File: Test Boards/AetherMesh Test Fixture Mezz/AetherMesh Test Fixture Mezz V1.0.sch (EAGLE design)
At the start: 7 parts, among them J1 POWER_JACKEJ508A, M1 AETHERMESH_MODULEMEZZ-HOLES

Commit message: Re-organized test fixture boards and corrected part number attributes
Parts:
- S1, S2: MFG# 4882 -> 9774040243R
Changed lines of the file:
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@@
 <?xml version="1.0" encoding="utf-8"?>
 <!DOCTYPE eagle SYSTEM "eagle.dtd">
-<eagle version="8.3.1">
+<eagle version="8.3.2">
 <drawing>
 <settings>
@@
 <part name="M1" library="AetherConnectivity" deviceset="AETHERMESH_MODULE" device="MEZZ-HOLES"/>
 <part name="S1" library="AetherConnectivity" deviceset="STANDOFF" device="WURTH">
-<attribute name="MFG#" value="4882"/>
+<attribute name="MFG#" value="9774040243R"/>
 </part>
 <part name="S2" library="AetherConnectivity" deviceset="STANDOFF" device="WURTH">
-<attribute name="MFG#" value="4882"/>
+<attribute name="MFG#" value="9774040243R"/>
 </part>
 <part name="GND2" library="3. growflux" library_urn="urn:adsk.eagle:library:207379" deviceset="GND" device=""/>

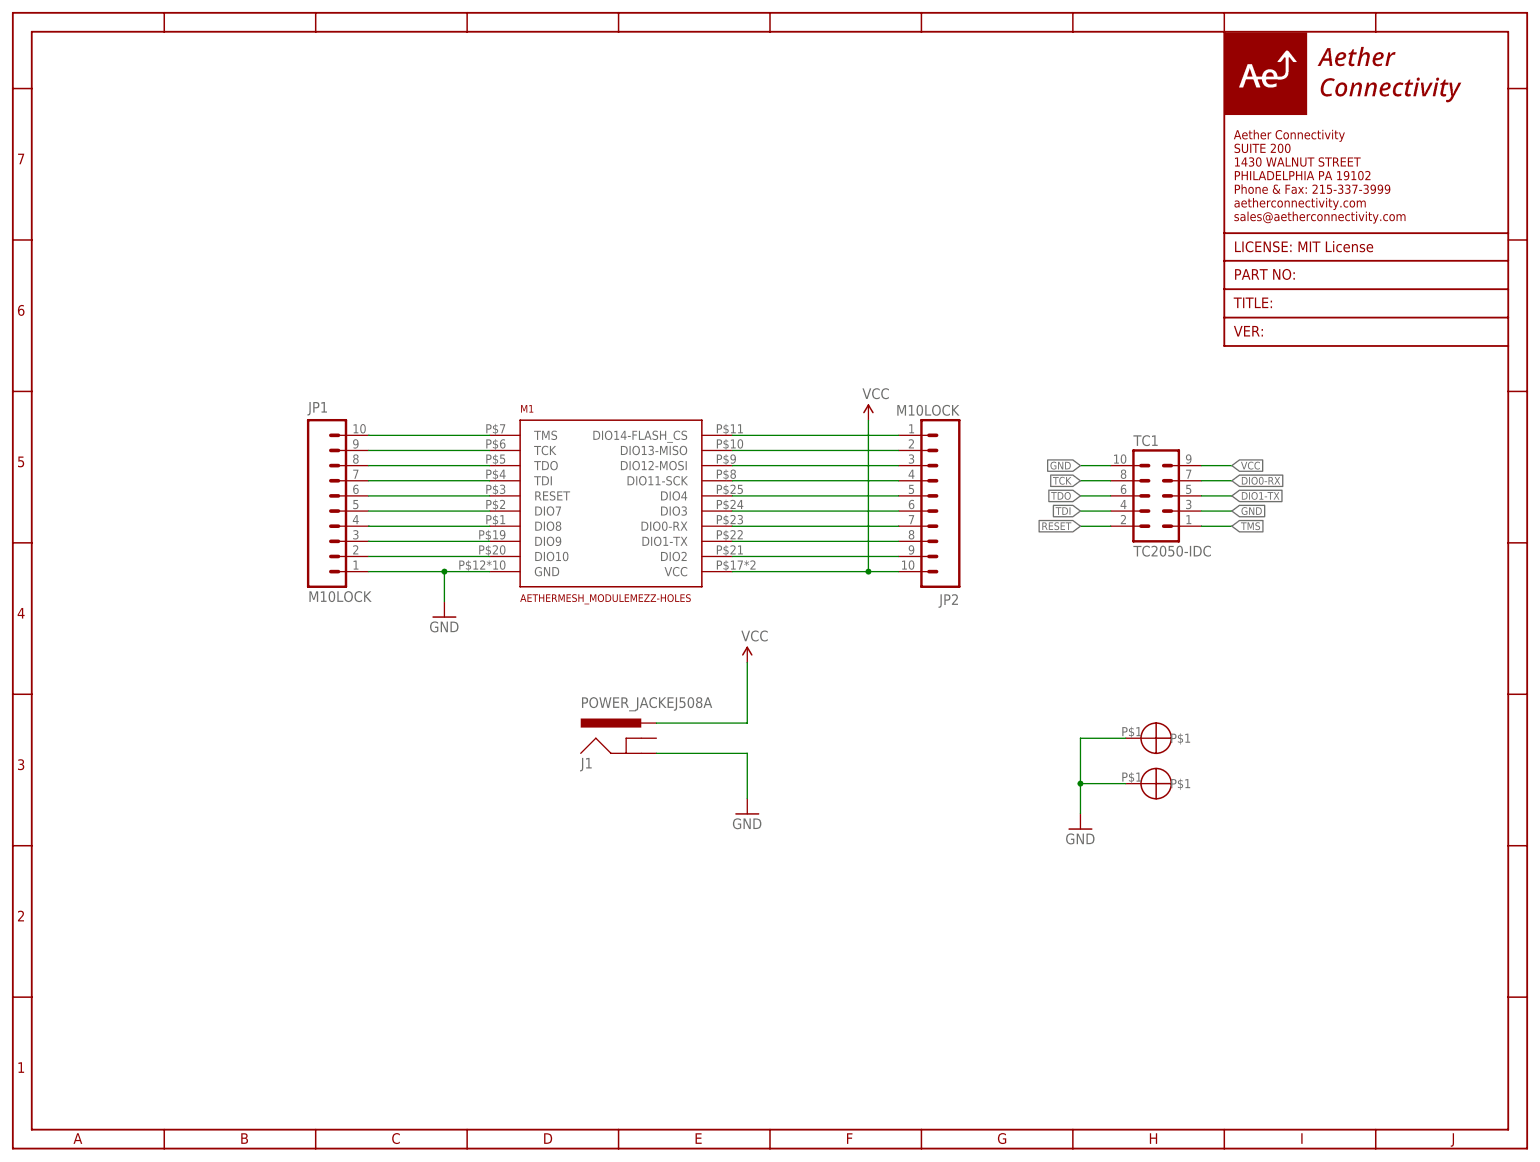
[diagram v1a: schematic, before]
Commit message: Updated test boards with silkscreen pin names and current measurment jumper
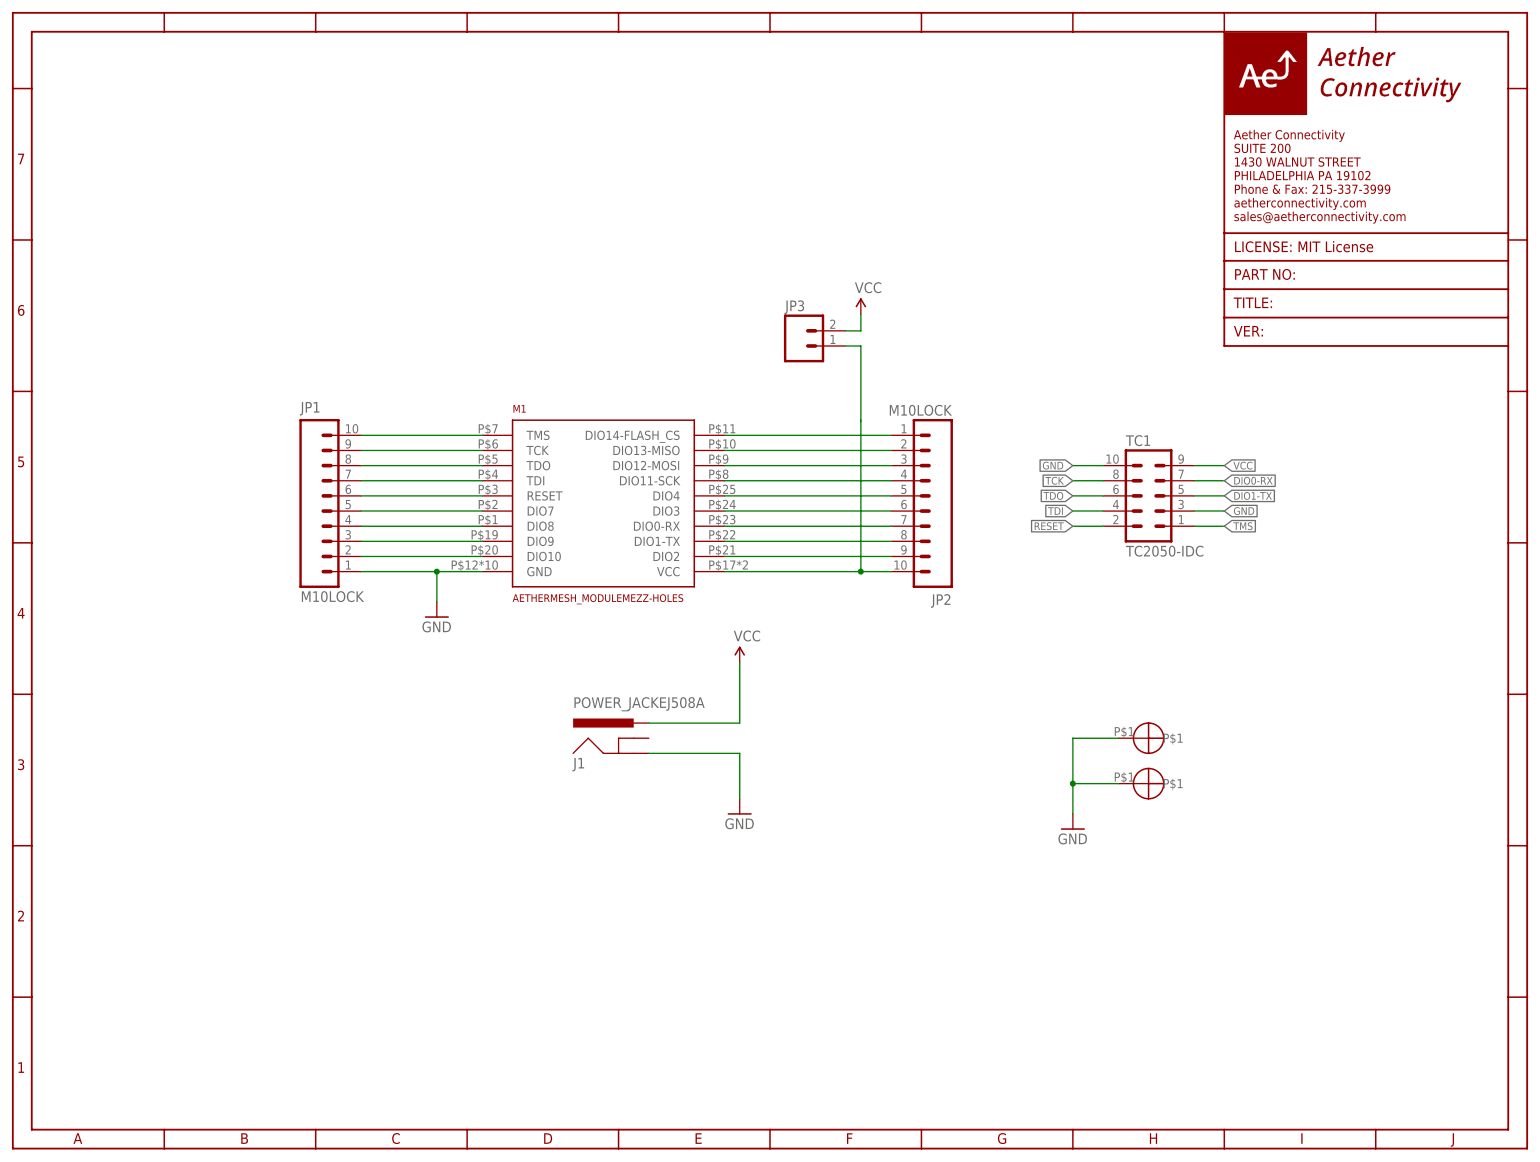
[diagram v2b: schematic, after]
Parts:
- added JP3: (no value), 1. growflux:M02LOCK
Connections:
- new net N$3: JP2.10, JP3.1, M1.VCC
- net VCC: now also JP3.2; no longer JP2.10, M1.VCC
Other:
- moved on the sheet: J1, JP1, JP2, M1, TC1
